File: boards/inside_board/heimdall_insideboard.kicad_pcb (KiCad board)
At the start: 2 copper layers, 150 x 100 mm, 58 parts, among them J1 Barrel_Jack_Switch, J2 Screw_Terminal_01x04, J3 Conn_01x09, J4 Screw_Terminal_01x04, J5 Conn_01x09, J6 Screw_Terminal_01x04, J7 Screw_Terminal_01x06, J8 Screw_Terminal_01x09, J9 Screw_Terminal_01x02, K1 Relay_HJR-3FF-S-Z-5VDC, K2 Relay_HJR-3FF-S-Z-5VDC, K3 Relay_HJR-3FF-S-Z-5VDC, Q1 2N3904, Q2 2N3904, Q3 2N3904, Q4 2N3904, Q5 2N3904, U1 LM1117-3.3, U2 L7805, U3 ESP32_Dev_Board_30Pin

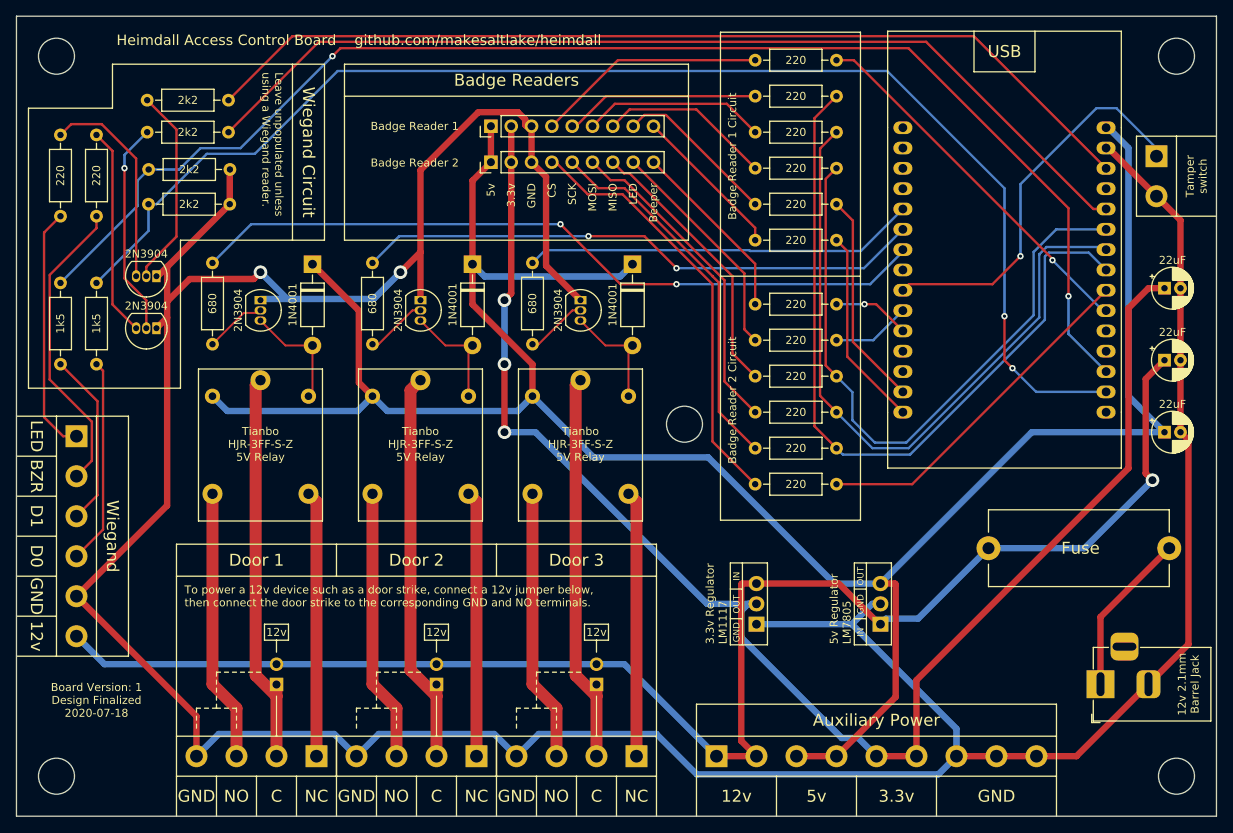
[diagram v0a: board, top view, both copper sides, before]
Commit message: update the inside board PCB design file
a number of changes:

 - add an extra terminal to the wiegand header for the 26/34 mode
   switching pin that most wiegand readers have, complete with a
   jumper to selectively connect that terminal to ground
 - expand screw terminal silkscreen outline to fit the actual size
   of the screw terminals; i misread the datasheet when laying them
   out in the previous board revision
 - move the 5v regulator .2" to the right so that there's more
   clearance between it and the 3.3v one when the heatsinks are
   attached
 - correspondingly, move the ESP32 left by about .1" to make room
   for the tamper switch screw terminal's actual size
 - move neighboring resistors closer since they fit well within
   their component outline
 - change the transistor footprint to one with wider spacing, for
   ease of soldering by volunteers
 - add labels for the 12v plug and the fuse that can still be seen
   once the components are installed
 - add a through-hole addressable RGB LED for board status
   signalling and other shenanigans
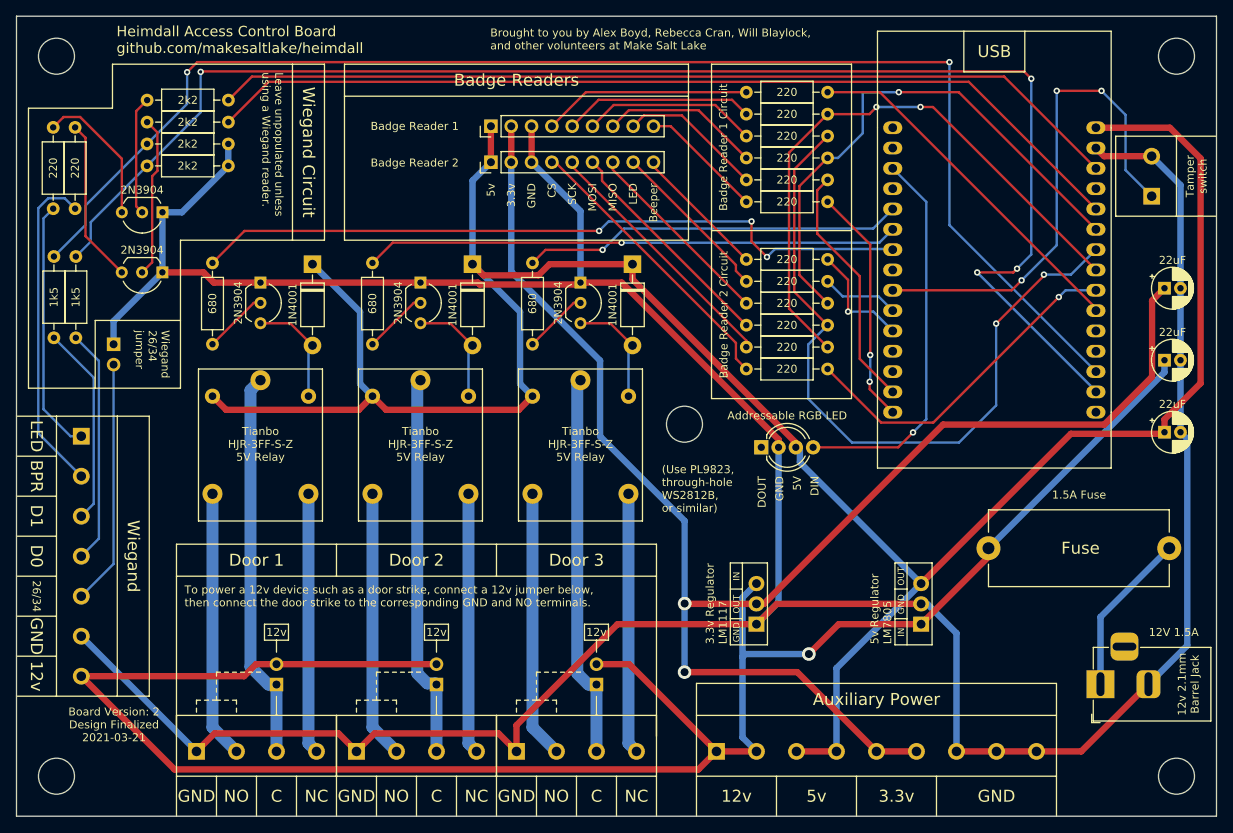
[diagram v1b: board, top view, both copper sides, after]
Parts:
- removed Q3, Q4, Q5: 2N3904, Javawizard_Common_Footprints:JW_TO-92_Inline_Silkscreen_Part_Number_Only
- added 2N3904: 2N3904, Javawizard_Common_Footprints:JW_TO-92_Inline_Wide_Silkscreen_Part_Number_Only, F.Cu at (43.2, 57.0)
- added 2N3904: 2N3904, Javawizard_Common_Footprints:JW_TO-92_Inline_Wide_Silkscreen_Part_Number_Only, F.Cu at (43.2, 49.5)
- added 2N3904: 2N3904, Javawizard_Common_Footprints:JW_TO-92_Inline_Wide_Silkscreen_Part_Number_Only, F.Cu at (95.5, 58.3)
- added Addressable RGB LED: NeoPixel_THT, LED_THT:LED_D5.0mm-4_RGB_Wide_Pins, F.Cu at (118.1, 78.9)
- added JP4: Jumper, Javawizard_Common_Footprints:PinHeader_JW_1x02_P2.54mm_Vertical_Without_Silkscreen, F.Cu at (37.1, 66.0)
- 2N3904: renamed from Q2; footprint Javawizard_Common_Footprints:JW_TO-92_Inline_Silkscreen_Part_Number_Only -> Javawizard_Common_Footprints:JW_TO-92_Inline_Wide_Silkscreen_Part_Number_Only
- 2N3904: renamed from Q1; footprint Javawizard_Common_Footprints:JW_TO-92_Inline_Silkscreen_Part_Number_Only -> Javawizard_Common_Footprints:JW_TO-92_Inline_Wide_Silkscreen_Part_Number_Only
- J7: footprint Javawizard_Common_Footprints:PinHeader_JW_1x06_P5.00mm_Vertical -> Javawizard_Common_Footprints:PinHeader_JW_1x07_P5.00mm_Vertical
- moved J2 15.0 mm to (47.5, 116.9), turned to 90 degrees
- moved J4 15.0 mm to (67.5, 116.9), turned to 90 degrees
- moved J6 15.0 mm to (87.5, 116.9), turned to 90 degrees
- moved R9 14.4 mm to (126.4, 69.1)
- moved R10 12.7 mm to (126.4, 66.4)
- moved R11 10.9 mm to (126.4, 63.6)
- moved R12 9.19 mm to (126.4, 60.9)
- moved R13 7.44 mm to (126.4, 58.1)
- moved R14 5.71 mm to (126.4, 55.4)
- moved U2 5.08 mm to (138.1, 101.0)
- moved J9 5.04 mm to (166.9, 47.5), turned to 180 degrees
- moved R8 4.93 mm to (126.4, 48.2)
- moved R23 4.79 mm to (41.3, 43.7)
- moved R17 4.19 mm to (32.4, 65.2)
- moved R2 4.15 mm to (126.4, 34.5)
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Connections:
- J2 pad 1: /RELAY1_NC -> GND
- J2 pad 2: /RELAY1_C -> /RELAY1_NO
- J2 pad 3: /RELAY1_NO -> /RELAY1_C
- J2 pad 4: GND -> /RELAY1_NC
- J4 pad 1: /RELAY2_NC -> GND
- J4 pad 2: /RELAY2_C -> /RELAY2_NO
- J4 pad 3: /RELAY2_NO -> /RELAY2_C
- J4 pad 4: GND -> /RELAY2_NC
- J6 pad 1: /RELAY3_NC -> GND
- J6 pad 2: /RELAY3_C -> /RELAY3_NO
- J6 pad 3: /RELAY3_NO -> /RELAY3_C
- J6 pad 4: GND -> /RELAY3_NC
- J7 pad 5: GND -> Net-(J7-Pad5)
- J7 pad 6: +12V -> GND
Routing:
- net +12V: track 190.8 -> 246.7 mm
- net Net-(D4-Pad4): track 0.00 -> 48.7 mm, vias 0 -> 1
- net Net-(J7-Pad5): track 0.00 -> 30.6 mm
- net Net-(R10-Pad1): track 96.3 -> 75.5 mm, vias 0 -> 2
- net GND: track 433.2 -> 414.3 mm, vias 2 -> 0
- net Net-(J5-Pad4): track 53.7 -> 36.2 mm
- net Net-(R17-Pad2): track 168.3 -> 184.5 mm, vias 2 -> 4
- net Net-(J5-Pad5): track 47.2 -> 32.1 mm
- net Net-(J9-Pad1): track 49.5 -> 63.5 mm, vias 1 -> 3
- net Net-(R12-Pad1): track 82.0 -> 68.1 mm, vias 0 -> 1
- net Net-(J5-Pad6): track 40.7 -> 28.3 mm
- net Net-(Q4-Pad2): track 25.1 -> 14.9 mm
- net Net-(J5-Pad7): track 34.5 -> 24.5 mm
- net Net-(Q4-Pad3): track 26.5 -> 18.0 mm
- net Net-(J5-Pad8): track 28.6 -> 20.7 mm
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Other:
- net class Default: clearance 0.2 -> 0.35
- net class Power: clearance 0.2 -> 0.35
- rule pad_to_mask_clearance: 0.05 -> 0
- rule trace_clearance: 0.2 -> 0.35
- rule trace_min: 0.2 -> 0.25
- board text added: "(Use PL9823, through-hole WS2812B, or similar)"
- board text added: "1.5A Fuse"
- board text added: "12V 1.5A"
- board text added: "26/34"
- board text added: "5V"
- board text added: "BPR"
- board text added: "Board Version: 2 Design Finalized 2021-03-21"
- board text added: "Brought to you by Alex Boyd, Rebecca Cran, Will Blaylock, and other volunteers at Make Salt Lake"
- board text added: "DIN"
- board text added: "DOUT"
- board text added: "Wiegand 26/34 jumper"
- board text removed: "BZR"
- board text removed: "Board Version: 1 Design Finalized 2020-07-18"
